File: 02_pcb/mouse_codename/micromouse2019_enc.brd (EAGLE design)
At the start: 5.9 x 11.1 mm, 7 parts, among them IC1 AS5047D

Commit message: encoder pcb updated
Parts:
- IC1: device parts_not_managed:SOP65P640X120-14N -> parts:SOP65P640X120-14N
- PORT1: device parts_not_managed:ENC_PORT_MODULE -> parts:ENC_PORT_MODULE
- SPI: device parts_not_managed:PINHD4-1.27 -> parts:PINHD4-1.27
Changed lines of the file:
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@@
 <drawing>
 <settings>
-<setting alwaysvectorfont="no"/>
+<setting alwaysvectorfont="yes"/>
 <setting verticaltext="up"/>
 </settings>
@@
 <layer number="48" name="Document" color="7" fill="1" visible="yes" active="yes"/>
 <layer number="49" name="Reference" color="7" fill="1" visible="yes" active="yes"/>
+<layer number="50" name="dxf" color="7" fill="1" visible="no" active="no"/>
 <layer number="51" name="tDocu" color="7" fill="1" visible="yes" active="yes"/>
 <layer number="52" name="bDocu" color="7" fill="1" visible="yes" active="yes"/>
+<layer number="53" name="tGND_GNDA" color="7" fill="9" visible="no" active="no"/>
+<layer number="54" name="bGND_GNDA" color="1" fill="9" visible="no" active="no"/>
+<layer number="56" name="wert" color="7" fill="1" visible="no" active="no"/>
+<layer number="57" name="tCAD" color="7" fill="1" visible="no" active="no"/>
+<layer number="59" name="tCarbon" color="7" fill="1" visible="no" active="no"/>
+<layer number="60" name="bCarbon" color="7" fill="1" visible="no" active="no"/>
 <layer number="88" name="SimResults" color="9" fill="1" visible="no" active="no"/>
 <layer number="89" name="SimProbes" color="9" fill="1" visible="no" active="no"/>
@@
 <layer number="97" name="Info" color="7" fill="1" visible="no" active="no"/>
 <layer number="98" name="Guide" color="6" fill="1" visible="no" active="no"/>
+<layer number="99" name="SpiceOrder" color="7" fill="1" visible="no" active="no"/>
+<layer number="100" name="Muster" color="7" fill="1" visible="no" active="no"/>
+<layer number="101" name="Patch_Top" color="12" fill="4" visible="no" active="yes"/>
+<layer number="102" name="Vscore" color="7" fill="1" visible="no" active="yes"/>
+<layer number="103" name="fp3" color="7" fill="1" visible="no" active="yes"/>
+<layer number="104" name="Name" color="7" fill="1" visible="no" active="yes"/>
+<layer number="105" name="Beschreib" color="9" fill="1" visible="no" active="yes"/>
+<layer number="106" name="BGA-Top" color="4" fill="1" visible="no" active="yes"/>
+<layer number="107" name="BD-Top" color="5" fill="1" visible="no" active="yes"/>
+<layer number="108" name="fp8" color="7" fill="1" visible="no" active="yes"/>
+<layer number="109" name="fp9" color="7" fill="1" visible="no" active="yes"/>
+<layer number="110" name="fp0" color="7" fill="1" visible="no" active="yes"/>
+<layer number="111" name="LPC17xx" color="7" fill="1" visible="no" active="yes"/>
+<layer number="112" name="tSilk" color="7" fill="1" visible="no" active="yes"/>
+<layer number="113" name="ReferenceLS" color="7" fill="1" visible="no" active="no"/>
+<layer number="116" name="Patch_BOT" color="9" fill="4" visible="no" active="yes"/>
+<layer number="118" name="Rect_Pads" color="7" fill="1" visible="no" active="no"/>
+<layer number="121" name="_tsilk" color="7" fill="1" visible="no" active="yes"/>
+<layer number="122" name="_bsilk" color="7" fill="1" visible="no" active="yes"/>
+<layer number="123" name="tTestmark" color="7" fill="1" visible="no" active="yes"/>
+<layer number="124" name="bTestmark" color="7" fill="1" visible="no" active="yes"/>
+<layer number="125" name="_tNames" color="7" fill="1" visible="no" active="yes"/>
+<layer number="126" name="_bNames" color="7" fill="1" visible="no" active="yes"/>
+<layer number="127" name="_tValues" color="7" fill="1" visible="no" active="yes"/>
+<layer number="128" name="_bValues" color="7" fill="1" visible="no" active="yes"/>
+<layer number="129" name="Mask" color="7" fill="1" visible="yes" active="yes"/>
+<layer number="131" name="tAdjust" color="7" fill="1" visible="no" active="yes"/>
+<layer number="132" name="bAdjust" color="7" fill="1" visible="no" active="yes"/>
+<layer number="144" name="Drill_legend" color="7" fill="1" visible="no" active="yes"/>
+<layer number="150" name="Notes" color="7" fill="1" visible="no" active="yes"/>
+<layer number="151" name="HeatSink" color="7" fill="1" visible="no" active="yes"/>
+<layer number="152" name="_bDocu" color="7" fill="1" visible="no" active="yes"/>
+<layer number="153" name="FabDoc1" color="6" fill="1" visible="no" active="no"/>
+<layer number="154" name="FabDoc2" color="2" fill="1" visible="no" active="no"/>
+<layer number="155" name="FabDoc3" color="7" fill="15" visible="no" active="no"/>
+<layer number="199" name="Contour" color="7" fill="1" visible="no" active="yes"/>
+<layer number="200" name="200bmp" color="1" fill="10" visible="no" active="yes"/>
+<layer number="201" name="201bmp" color="2" fill="1" visible="no" active="no"/>
+<layer number="202" name="202bmp" color="3" fill="1" visible="no" active="no"/>
+<layer number="203" name="203bmp" color="4" fill="10" visible="no" active="yes"/>
+<layer number="204" name="204bmp" color="5" fill="10" visible="no" active="yes"/>
+<layer number="205" name="205bmp" color="6" fill="10" visible="no" active="yes"/>
+<layer number="206" name="206bmp" color="7" fill="10" visible="no" active="yes"/>
+<layer number="207" name="207bmp" color="8" fill="10" visible="no" active="yes"/>
+<layer number="208" name="208bmp" color="9" fill="10" visible="no" active="yes"/>
+<layer number="209" name="209bmp" color="7" fill="1" visible="no" active="yes"/>
+<layer number="210" name="210bmp" color="7" fill="1" visible="no" active="yes"/>
+<layer number="211" name="211bmp" color="7" fill="1" visible="no" active="yes"/>
+<layer number="212" name="212bmp" color="7" fill="1" visible="no" active="yes"/>
+<layer number="213" name="213bmp" color="7" fill="1" visible="no" active="yes"/>
+<layer number="214" name="214bmp" color="7" fill="1" visible="no" active="yes"/>
+<layer number="215" name="215bmp" color="7" fill="1" visible="no" active="yes"/>
+<layer number="216" name="216bmp" color="7" fill="1" visible="no" active="yes"/>
+<layer number="217" name="217bmp" color="18" fill="1" visible="no" active="no"/>
+<layer number="218" name="218bmp" color="19" fill="1" visible="no" active="no"/>
+<layer number="219" name="219bmp" color="20" fill="1" visible="no" active="no"/>
+<layer number="220" name="220bmp" color="21" fill="1" visible="no" active="no"/>
+<layer number="221" name="221bmp" color="22" fill="1" visible="no" active="no"/>
+<layer number="222" name="222bmp" color="23" fill="1" visible="no" active="no"/>
+<layer number="223" name="223bmp" color="24" fill="1" visible="no" active="no"/>
+<layer number="224" name="224bmp" color="25" fill="1" visible="no" active="no"/>
+<layer number="225" name="225bmp" color="7" fill="1" visible="yes" active="yes"/>
+<layer number="226" name="226bmp" color="7" fill="1" visible="yes" active="yes"/>
+<layer number="227" name="227bmp" color="7" fill="1" visible="yes" active="yes"/>
+<layer number="228" name="228bmp" color="7" fill="1" visible="yes" active="yes"/>
+<layer number="229" name="229bmp" color="7" fill="1" visible="yes" active="yes"/>
+<layer number="230" name="230bmp" color="7" fill="1" visible="yes" active="yes"/>
+<layer number="231" name="Eagle3D_PG1" color="7" fill="1" visible="no" active="no"/>
+<layer number="232" name="Eagle3D_PG2" color="7" fill="1" visible="no" active="no"/>
+<layer number="233" name="Eagle3D_PG3" color="7" fill="1" visible="no" active="no"/>
+<layer number="248" name="Housing" color="7" fill="1" visible="no" active="yes"/>
+<layer number="249" name="Edge" color="7" fill="1" visible="no" active="yes"/>
+<layer number="250" name="Descript" color="7" fill="1" visible="no" active="no"/>
+<layer number="251" name="SMDround" color="7" fill="1" visible="no" active="no"/>
+<layer number="254" name="cooling" color="7" fill="1" visible="no" active="yes"/>
+<layer number="255" name="routoute" color="7" fill="1" visible="yes" active="yes"/>
 </layers>
 <board>
+<fusionsync huburn="a.cGVyc29uYWw6dWUyOWUzYzUy" projecturn="a.cGVyc29uYWw6dWUyOWUzYzUyIzIwMTkwMjExMTc1NjcyODUx" f3durn="urn:adsk.wipprod:dm.lineage:Rxm10mLTRvSe4zHQ0xKiHA" pcbguid="812d53ff-404d-449c-89ab-42e65b23e1ef" lastpulledtime="" lastsyncedchangeguid="feedeed4-1ef2-0792-c0b8-603b07f8e484"/>
 <plain>
 <wire x1="0" y1="11.11" x2="0" y2="0" width="0" layer="20"/>
@@
 </autorouter>
 <elements>
-<element name="IC1" library="parts_not_managed" package="SOP65P640X120-14N" value="AS5047D" x="2.95" y="5.51" smashed="yes" rot="R270">
+<element name="IC1" library="parts" library_urn="urn:adsk.eagle:library:8879268" package="SOP65P640X120-14N" package3d_urn="urn:adsk.eagle:package:9139945/3" value="AS5047D" x="2.95" y="5.51" smashed="yes" rot="R270">
 <attribute name="DESCRIPTION" value="ams AS5047D-ATSM Hall Effect Sensor 14-Pin TSSOP, 3  3.6 V, 4.5  5.5 V" x="2.95" y="5.51" size="1.778" layer="27" rot="R270" display="off"/>
 <attribute name="HEIGHT" value="1.2mm" x="2.95" y="5.51" size="1.778" layer="27" rot="R270" display="off"/>
@@
 <attribute name="VALUE" x="0.3856375" y="2.22838125" size="0.7" layer="28" rot="MR180"/>
 </element>
-<element name="SPI" library="parts_not_managed" package="PINHD4-1.27" value="CON_WIRE" x="2.9510375" y="10.43258125" smashed="yes" rot="R180"/>
-<element name="PORT1" library="parts_not_managed" package="ENC_PORT_MODULE" value="ENC_PORT_MODULE" x="2.95" y="0.5" smashed="yes">
+<element name="SPI" library="parts" library_urn="urn:adsk.eagle:library:8879268" package="PINHD4-1.27" package3d_urn="urn:adsk.eagle:package:9141217/3" value="CON_WIRE" x="2.9510375" y="10.43258125" smashed="yes" rot="R180"/>
+<element name="PORT1" library="parts" library_urn="urn:adsk.eagle:library:8879268" package="ENC_PORT_MODULE" package3d_urn="urn:adsk.eagle:package:9139944/2" value="ENC_PORT_MODULE" x="2.95" y="0.5" smashed="yes">
 <attribute name="VALUE" x="0.45" y="-0.931665625" size="0.7" layer="27"/>
 </element>
@@
 </note>
 <note version="8.3" severity="warning">
+Since Version 8.3, EAGLE supports Fusion synchronisation.
+This feature will not be available in this version and saving
+the document will break the link to the Fusion PCB feature.
+</note>
+<note version="8.3" severity="warning">

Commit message: encoder board libs replaced with 0-micromouse.lbr
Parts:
- C1: device rcl:C0402 -> 0-micromouse2019:C0402
- IC1: device parts:SOP65P640X120-14N -> 0-micromouse2019:SOP65P640X120-14N
- PORT1: device parts:ENC_PORT_MODULE -> 0-micromouse2019:ENC_PORT_MODULE
- R1, R2, R3: device rcl:R0402 -> 0-micromouse2019:R0402
- SPI: device parts:PINHD4-1.27 -> 0-micromouse2019:PINHD4-1.27
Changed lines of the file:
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@@
 <drawing>
 <settings>
-<setting alwaysvectorfont="yes"/>
+<setting alwaysvectorfont="no"/>
 <setting verticaltext="up"/>
 </settings>
@@
 </autorouter>
 <elements>
-<element name="IC1" library="parts" library_urn="urn:adsk.eagle:library:8879268" package="SOP65P640X120-14N" package3d_urn="urn:adsk.eagle:package:9139945/3" value="AS5047D" x="2.95" y="5.51" smashed="yes" rot="R270">
+<element name="IC1" library="0-micromouse2019" package="SOP65P640X120-14N" package3d_urn="urn:adsk.eagle:package:9139945/3" value="AS5047D" x="2.95" y="5.51" smashed="yes" rot="R270">
 <attribute name="DESCRIPTION" value="ams AS5047D-ATSM Hall Effect Sensor 14-Pin TSSOP, 3  3.6 V, 4.5  5.5 V" x="2.95" y="5.51" size="1.778" layer="27" rot="R270" display="off"/>
 <attribute name="HEIGHT" value="1.2mm" x="2.95" y="5.51" size="1.778" layer="27" rot="R270" display="off"/>
@@
 <attribute name="VALUE" x="2.999" y="1.3244" size="0.7" layer="27" align="center"/>
 </element>
-<element name="R1" library="rcl" library_urn="urn:adsk.eagle:library:334" package="R0402" package3d_urn="urn:adsk.eagle:package:23547/3" value="10k" x="4.8560375" y="5.60658125" smashed="yes" rot="MR270">
+<element name="R1" library="0-micromouse2019" package="R0402" package3d_urn="urn:adsk.eagle:package:23547/3" value="10k" x="4.8560375" y="5.60658125" smashed="yes" rot="MR270">
 <attribute name="NAME" x="4.395934375" y="9.21975625" size="0.7" layer="26" rot="MR180"/>
 <attribute name="SPICEPREFIX" value="R" x="4.8560375" y="5.60658125" size="1.778" layer="28" rot="MR270" display="off"/>
 <attribute name="VALUE" x="4.14701875" y="8.2342375" size="0.7" layer="28" rot="MR180"/>
 </element>
-<element name="R2" library="rcl" library_urn="urn:adsk.eagle:library:334" package="R0402" package3d_urn="urn:adsk.eagle:package:23547/3" value="10k" x="3.0780375" y="5.60658125" smashed="yes" rot="MR180">
+<element name="R2" library="0-micromouse2019" package="R0402" package3d_urn="urn:adsk.eagle:package:23547/3" value="10k" x="3.0780375" y="5.60658125" smashed="yes" rot="MR180">
 <attribute name="NAME" x="3.6783625" y="8.51581875" size="0.7" layer="26" rot="MR0"/>
 <attribute name="SPICEPREFIX" value="R" x="3.0780375" y="5.60658125" size="1.778" layer="28" rot="MR180" display="off"/>
 <attribute name="VALUE" x="3.78504375" y="7.525215625" size="0.7" layer="28" rot="MR0"/>
 </element>
-<element name="R3" library="rcl" library_urn="urn:adsk.eagle:library:334" package="R0402" package3d_urn="urn:adsk.eagle:package:23547/3" value="10k" x="1.0460375" y="6.11458125" smashed="yes" rot="MR90">
+<element name="R3" library="0-micromouse2019" package="R0402" package3d_urn="urn:adsk.eagle:package:23547/3" value="10k" x="1.0460375" y="6.11458125" smashed="yes" rot="MR90">
 <attribute name="NAME" x="1.77211875" y="8.49585625" size="0.7" layer="26" rot="MR0"/>
 <attribute name="SPICEPREFIX" value="R" x="1.0460375" y="6.11458125" size="1.778" layer="28" rot="MR90" display="off"/>
 <attribute name="VALUE" x="1.868640625" y="7.528115625" size="0.7" layer="28" rot="MR0"/>
 </element>
-<element name="C1" library="rcl" library_urn="urn:adsk.eagle:library:334" package="C0402" package3d_urn="urn:adsk.eagle:package:23626/2" value="100n" x="3.2050375" y="2.93958125" smashed="yes" rot="MR180">
+<element name="C1" library="0-micromouse2019" package="C0402" package3d_urn="urn:adsk.eagle:package:23626/2" value="100n" x="3.2050375" y="2.93958125" smashed="yes" rot="MR180">
 <attribute name="NAME" x="0.3856375" y="3.21898125" size="0.7" layer="26" rot="MR180"/>
 <attribute name="SPICEPREFIX" value="C" x="3.2050375" y="2.93958125" size="1.778" layer="28" rot="MR180" display="off"/>
 <attribute name="VALUE" x="0.3856375" y="2.22838125" size="0.7" layer="28" rot="MR180"/>
 </element>
-<element name="SPI" library="parts" library_urn="urn:adsk.eagle:library:8879268" package="PINHD4-1.27" package3d_urn="urn:adsk.eagle:package:9141217/3" value="CON_WIRE" x="2.9510375" y="10.43258125" smashed="yes" rot="R180"/>
-<element name="PORT1" library="parts" library_urn="urn:adsk.eagle:library:8879268" package="ENC_PORT_MODULE" package3d_urn="urn:adsk.eagle:package:9139944/2" value="ENC_PORT_MODULE" x="2.95" y="0.5" smashed="yes">
+<element name="SPI" library="0-micromouse2019" package="PINHD4-1.27" value="CON_WIRE" x="2.9510375" y="10.43258125" smashed="yes" rot="R180"/>
+<element name="PORT1" library="0-micromouse2019" package="ENC_PORT_MODULE" value="ENC_PORT_MODULE" x="2.95" y="0.5" smashed="yes">
 <attribute name="VALUE" x="0.45" y="-0.931665625" size="0.7" layer="27"/>
 </element>
@@
 </drawing>
 <compatibility>
-<note version="8.2" severity="warning">
-Since Version 8.2, EAGLE supports online libraries. The ids
-of those online libraries will not be understood (or retained)
-with this version.
-</note>
 <note version="8.3" severity="warning">
 Since Version 8.3, EAGLE supports Fusion synchronisation.

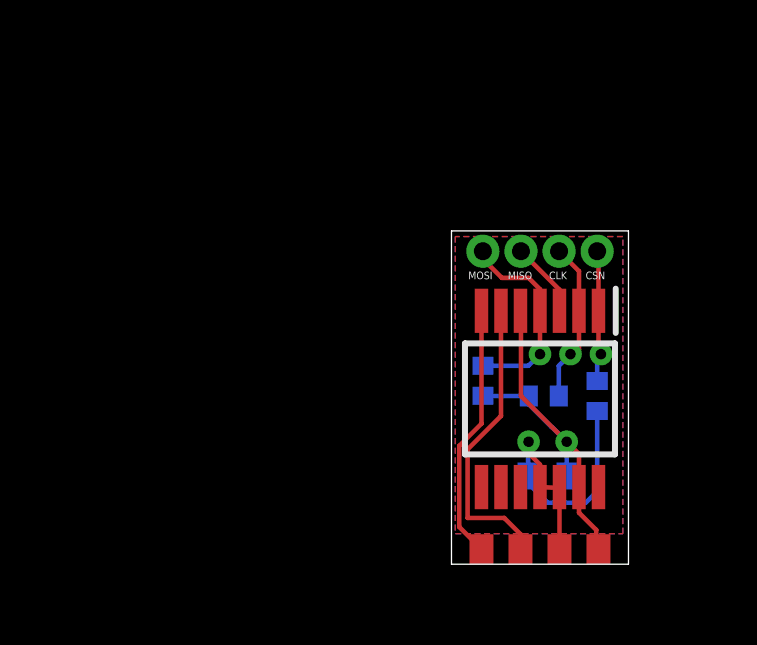
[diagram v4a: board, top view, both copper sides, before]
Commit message: Connectors replaced: IRDx4 & IRDVCC & SPI
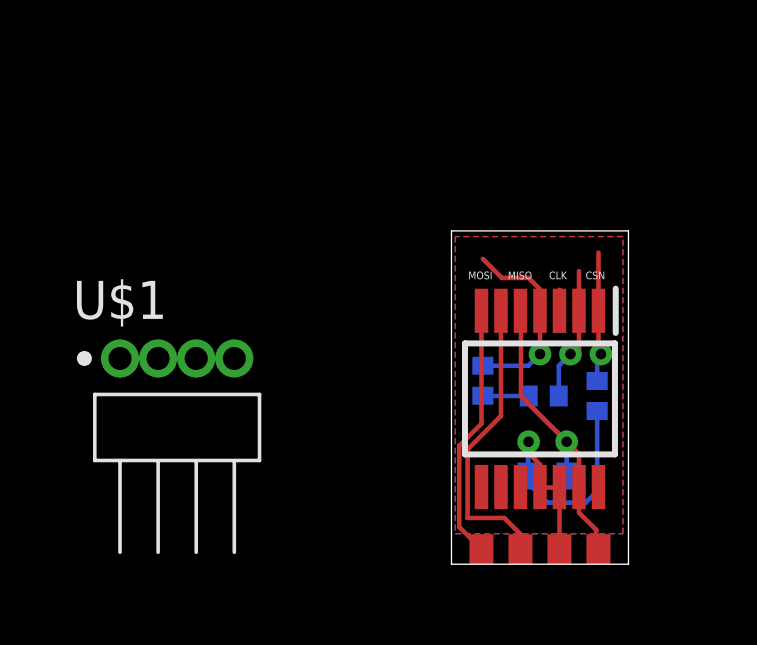
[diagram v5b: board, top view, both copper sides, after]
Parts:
- removed SPI: CON_WIRE, 0-micromouse2019:PINHD4-1.27
- added U$1: CONN_SPI, 0-micromouse2019:CONN_SPI_HDRRA4W40P127_1X4_549X220X220B
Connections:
- net CLK: now also U$1.3; no longer SPI.P2
- net CSN: now also U$1.4; no longer SPI.P1
- net MISO: now also U$1.2; no longer SPI.P3
- net MOSI: now also U$1.1; no longer SPI.P4
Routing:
- net MISO: track 2.52 -> 0.70 mm
- net CLK: track 5.45 -> 4.51 mm
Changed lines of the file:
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@@
 <attribute name="VALUE" x="0.3856375" y="2.22838125" size="0.7" layer="28" rot="MR180"/>
 </element>
-<element name="SPI" library="0-micromouse2019" package="PINHD4-1.27" value="CON_WIRE" x="2.9510375" y="10.43258125" smashed="yes" rot="R180"/>
 <element name="PORT1" library="0-micromouse2019" package="ENC_PORT_MODULE" value="ENC_PORT_MODULE" x="2.95" y="0.5" smashed="yes">
 <attribute name="VALUE" x="0.45" y="-0.931665625" size="0.7" layer="27"/>
+</element>
+<element name="U$1" library="0-micromouse2019" package="CONN_SPI_HDRRA4W40P127_1X4_549X220X220B" package3d_urn="urn:adsk.eagle:package:9165666/2" value="CONN_SPI" x="-11.049" y="6.858" smashed="yes">
+<attribute name="NAME" x="-11.049" y="8.1758" size="1.27" layer="25" align="bottom-center"/>
+<attribute name="VALUE" x="-11.049" y="-0.237" size="1.27" layer="27" align="top-center"/>
 </element>
 </elements>
@@
 <contactref element="IC1" pad="2"/>
 <contactref element="R2" pad="2"/>
-<contactref element="SPI" pad="P2"/>
 <wire x1="4.25" y1="8.448" x2="4.2510375" y2="7.16058125" width="0.1524" layer="1"/>
 <wire x1="4.2510375" y1="7.16058125" x2="4.0940375" y2="7.00358125" width="0.1524" layer="1"/>
@@
 <wire x1="3.5780375" y1="6.61458125" x2="3.9670375" y2="7.00358125" width="0.1524" layer="16"/>
 <wire x1="4.25" y1="8.448" x2="4.2510375" y2="9.76758125" width="0.1524" layer="1"/>
-<wire x1="4.2510375" y1="9.76758125" x2="3.5860375" y2="10.43258125" width="0.1524" layer="1"/>
+<contactref element="U$1" pad="3"/>
+<wire x1="-8.509" y1="6.858" x2="3.5780375" y2="6.61458125" width="0" layer="19" extent="16-16"/>
 </signal>
 <signal name="GND">
@@
 </signal>
 <signal name="CSN">
-<contactref element="SPI" pad="P1"/>
 <contactref element="IC1" pad="1"/>
 <contactref element="R1" pad="1"/>
@@
 <wire x1="4.8560375" y1="6.87658125" x2="4.8560375" y2="6.10658125" width="0.1524" layer="16"/>
 <wire x1="4.9" y1="8.448" x2="4.9010375" y2="10.38758125" width="0.1524" layer="1"/>
-<wire x1="4.9010375" y1="10.38758125" x2="4.8560375" y2="10.43258125" width="0.1524" layer="1"/>
+<contactref element="U$1" pad="4"/>
+<wire x1="-7.239" y1="6.858" x2="4.8560375" y2="6.87658125" width="0" layer="19" extent="16-16"/>
 </signal>
 <signal name="MISO">
-<contactref element="SPI" pad="P3"/>
 <contactref element="IC1" pad="3"/>
 <wire x1="3.6" y1="8.448" x2="3.6010375" y2="9.14758125" width="0.1524" layer="1"/>
-<wire x1="3.6010375" y1="9.14758125" x2="2.3160375" y2="10.43258125" width="0.1524" layer="1"/>
+<contactref element="U$1" pad="2"/>
+<wire x1="-9.779" y1="6.858" x2="3.6" y2="8.448" width="0" layer="19" extent="1-1"/>
 </signal>
 <signal name="MOSI">
-<contactref element="SPI" pad="P4"/>
 <contactref element="IC1" pad="4"/>
 <contactref element="R3" pad="2"/>
@@
 <wire x1="2.5700375" y1="9.54358125" x2="1.6810375" y2="9.54358125" width="0.1524" layer="1"/>
 <wire x1="1.6810375" y1="9.54358125" x2="1.0460375" y2="10.17858125" width="0.1524" layer="1"/>
-<wire x1="1.0460375" y1="10.17858125" x2="1.0460375" y2="10.43258125" width="0.1524" layer="1"/>
+<contactref element="U$1" pad="1"/>
+<wire x1="-11.049" y1="6.858" x2="1.0460375" y2="6.61458125" width="0" layer="19" extent="16-16"/>
 </signal>
 </signals>

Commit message: Enc pcb updated, design rules trace to dim updated
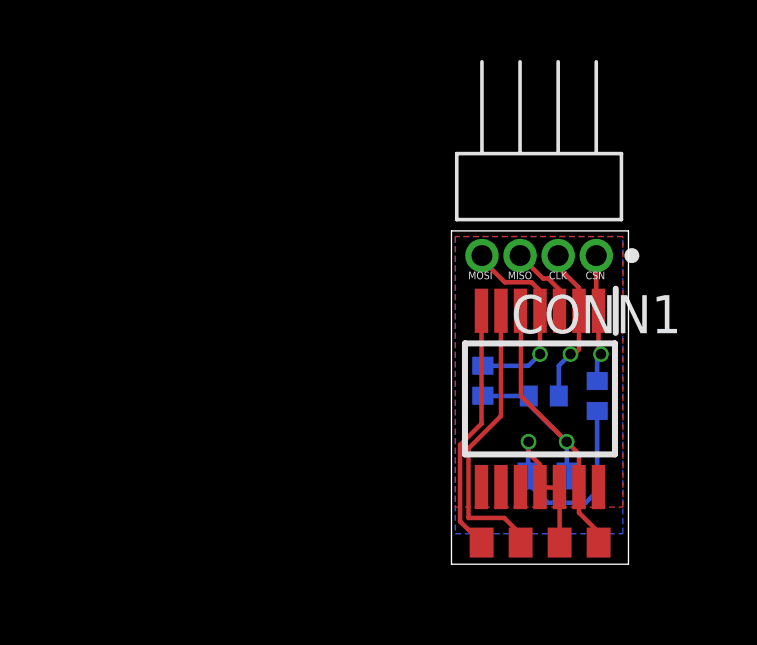
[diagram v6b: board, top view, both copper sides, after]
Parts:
- removed U$1: CONN_SPI, 0-micromouse2019:CONN_SPI_HDRRA4W40P127_1X4_549X220X220B
- added CONN1: CONN_SPI-P127, 0-micromouse2019:CONN_SPI_HDRRA4W40P127_1X4_549X220X220B
- PORT1: value ENC_PORT_MODULE -> PORT_ENC_MODULE
- moved PORT1 0.22 mm to (2.96, 0.72)
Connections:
- net CLK: now also CONN1.2; no longer U$1.3
- net CSN: now also CONN1.1; no longer U$1.4
- net MISO: now also CONN1.3; no longer U$1.2
- net MOSI: now also CONN1.4; no longer U$1.1
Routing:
- net MISO: track 0.70 -> 2.49 mm
- net CLK: track 4.51 -> 5.32 mm
